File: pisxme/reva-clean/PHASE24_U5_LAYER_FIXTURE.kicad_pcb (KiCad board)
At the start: 6 copper layers, 300 x 180 mm, 97 parts, among them J1 74221-101LF, J2 A70-112-331N126, J3 JAE SM3ZS067U410ABR1000 B-key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, J4 Amphenol 10171746-00021LF USB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, J5 0039300020, J6 0039300020, J7 Raspberry-Pi-5-Compute-Module, Q1 CSD19536KCS, Q2 CSD19536KCS, U1 LM74700QDBVRQ1, U2 LM74700QDBVRQ1, U3 TPSM63606RDLR, U4 TPSM63606RDLR, U5 TPSM63606RDLR, U6 TPD4EUSB30, U7 TUSB9261IPVP, U8 Texas_DRT_3, U9 TPD4EUSB30

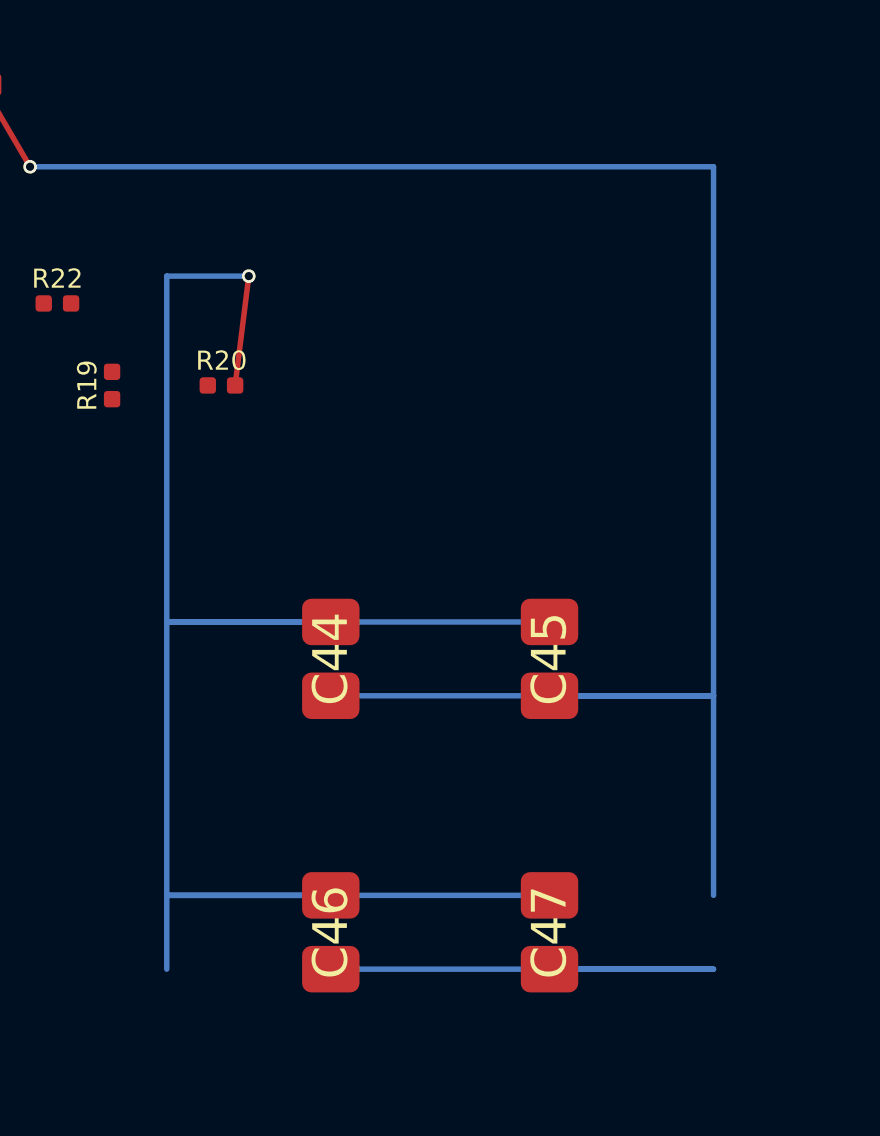
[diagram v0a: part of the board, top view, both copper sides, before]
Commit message: phase24 correct u5 layer fixture
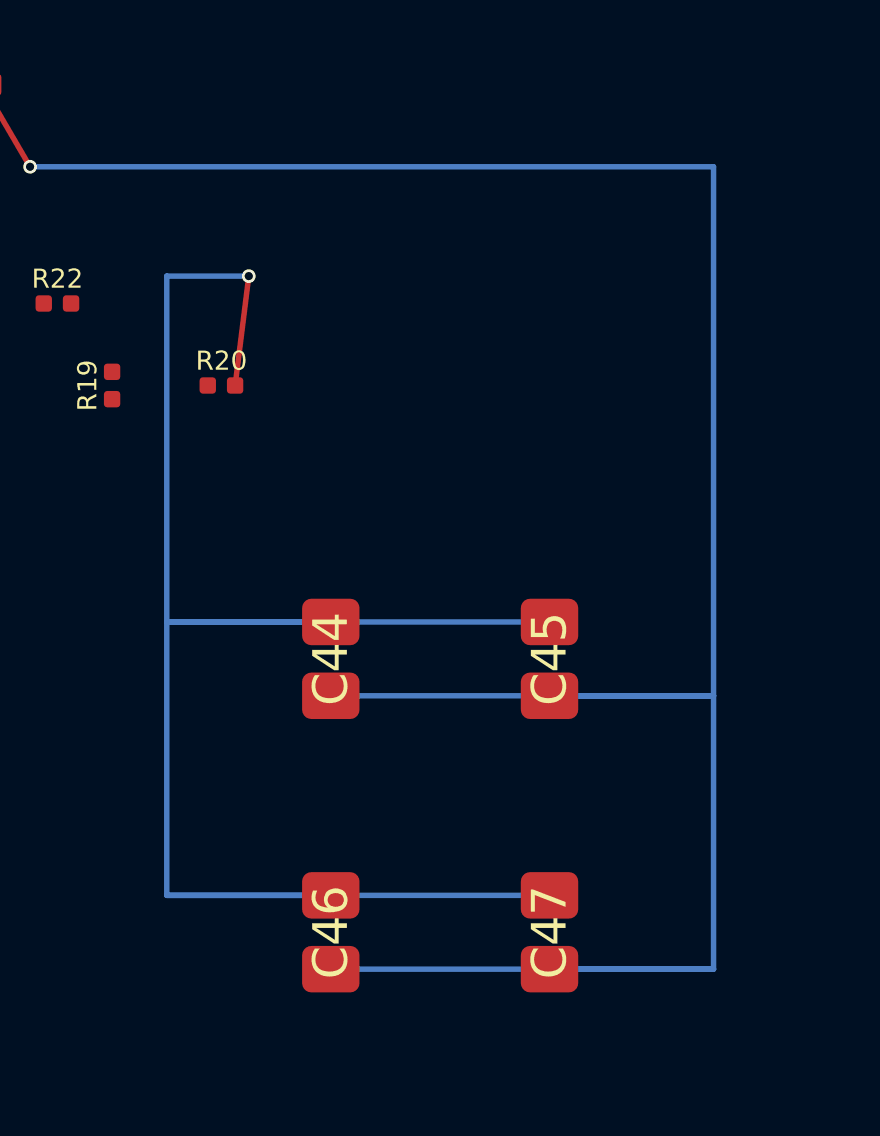
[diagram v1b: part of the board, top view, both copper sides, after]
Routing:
- net POWER_GND: track 72.4 -> 69.7 mm
- net /REGULATORS/BRIDGE_1V1: track 95.1 -> 97.8 mm
